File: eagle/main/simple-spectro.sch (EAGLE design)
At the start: 50 parts, among them IC1 MCP1703-33, Q1 DMP1045U, U1 MCP73831T, X2 8MHz, X4 MINI-USB

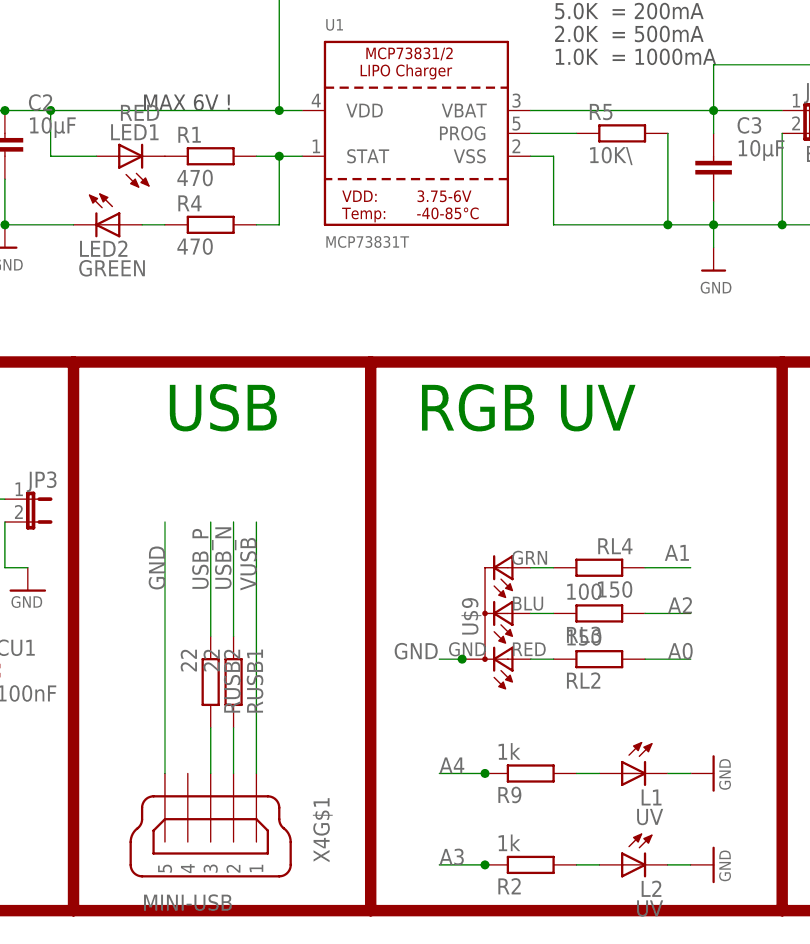
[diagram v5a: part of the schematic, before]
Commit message: update pcb values
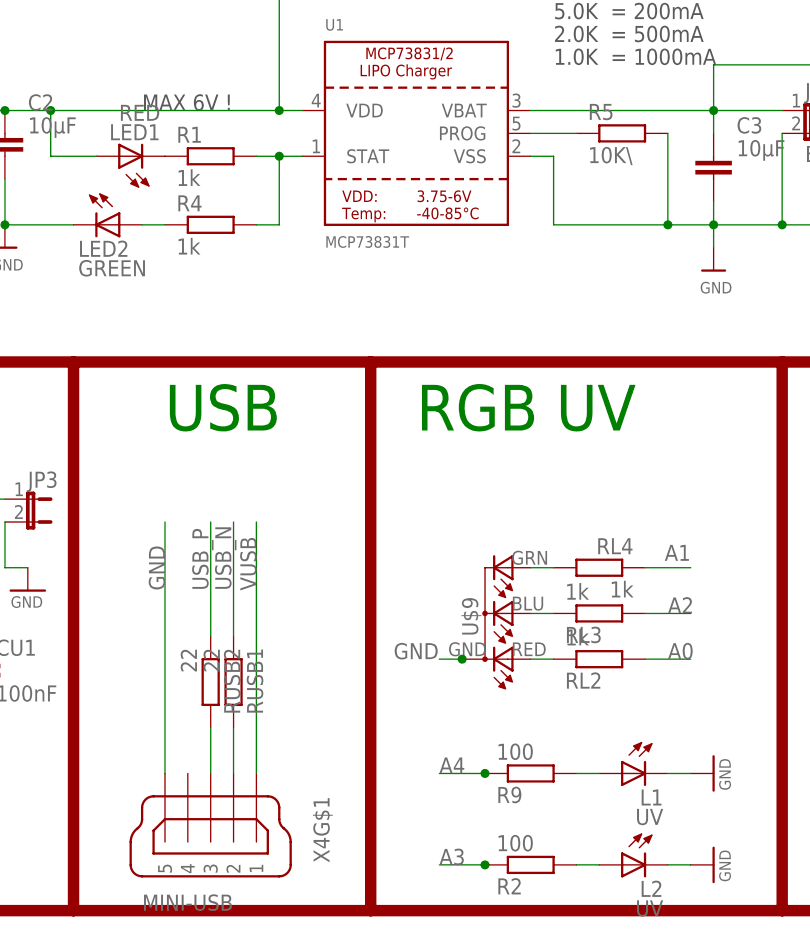
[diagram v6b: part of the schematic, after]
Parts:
- R1, R4: value 470 -> 1k
- R2, R9: value 1k -> 100
- RL2, RL4: value 150 -> 1k
- RL3: value 100 -> 1k
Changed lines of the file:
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@@
 <part name="LED1" library="SparkFun" deviceset="LED" device="1206" value="RED"/>
 <part name="LED2" library="SparkFun" deviceset="LED" device="1206" value="GREEN"/>
-<part name="R1" library="rcl" deviceset="R-EU_" device="M1206" package3d_urn="urn:adsk.eagle:package:23566/1" value="470"/>
-<part name="R4" library="rcl" deviceset="R-EU_" device="M1206" package3d_urn="urn:adsk.eagle:package:23566/1" value="470"/>
+<part name="R1" library="rcl" deviceset="R-EU_" device="M1206" package3d_urn="urn:adsk.eagle:package:23566/1" value="1k"/>
+<part name="R4" library="rcl" deviceset="R-EU_" device="M1206" package3d_urn="urn:adsk.eagle:package:23566/1" value="1k"/>
 <part name="C2" library="dp_devices" deviceset="CAPACITOR_NPOL" device="-1206" value="10µF"/>
 <part name="U$3" library="microbuilder" deviceset="GND" device=""/>
@@
 <part name="U$5" library="microbuilder" deviceset="GND" device=""/>
 <part name="R5" library="rcl" deviceset="R-EU_" device="M1206" package3d_urn="urn:adsk.eagle:package:23566/1" value="10K\"/>
-<part name="RL2" library="rcl" deviceset="R-EU_" device="M1206" value="150"/>
-<part name="RL3" library="rcl" deviceset="R-EU_" device="M1206" value="100"/>
-<part name="RL4" library="rcl" deviceset="R-EU_" device="M1206" value="150"/>
+<part name="RL2" library="rcl" deviceset="R-EU_" device="M1206" value="1k"/>
+<part name="RL3" library="rcl" deviceset="R-EU_" device="M1206" value="1k"/>
+<part name="RL4" library="rcl" deviceset="R-EU_" device="M1206" value="1k"/>
 <part name="U$9" library="lpatiny" deviceset="RGB-COMMON-CATHODE" device=""/>
 <part name="U$11" library="HD44780LCD" deviceset="LCD-HD44780" device="16X2-4-HOLES" technology="4-HOLES"/>
@@
 <part name="U$2" library="MyPOW" deviceset="VUSB" device=""/>
 <part name="D4" library="lpatiny" deviceset="1N581*" device="D1206" value="1N581D1206"/>
-<part name="R9" library="rcl" deviceset="R-EU_" device="M1206" value="1k"/>
+<part name="R9" library="rcl" deviceset="R-EU_" device="M1206" value="100"/>
 <part name="GND9" library="supply1" deviceset="GND" device=""/>
 <part name="L1" library="SparkFun" deviceset="LED" device="5MM" value="UV"/>
@@
 <part name="CU1" library="resistor" library_urn="urn:adsk.eagle:library:348" deviceset="C-EU" device="C1206" package3d_urn="urn:adsk.eagle:package:26140/1" value="100nF"/>
 <part name="RK3" library="rcl" library_urn="urn:adsk.eagle:library:334" deviceset="R-EU_" device="M1206" package3d_urn="urn:adsk.eagle:package:23566/1" value="100k"/>
-<part name="R2" library="rcl" deviceset="R-EU_" device="M1206" value="1k"/>
+<part name="R2" library="rcl" deviceset="R-EU_" device="M1206" value="100"/>
 <part name="GND10" library="supply1" deviceset="GND" device=""/>
 <part name="L2" library="led" deviceset="LED" device="3MM" value="UV"/>

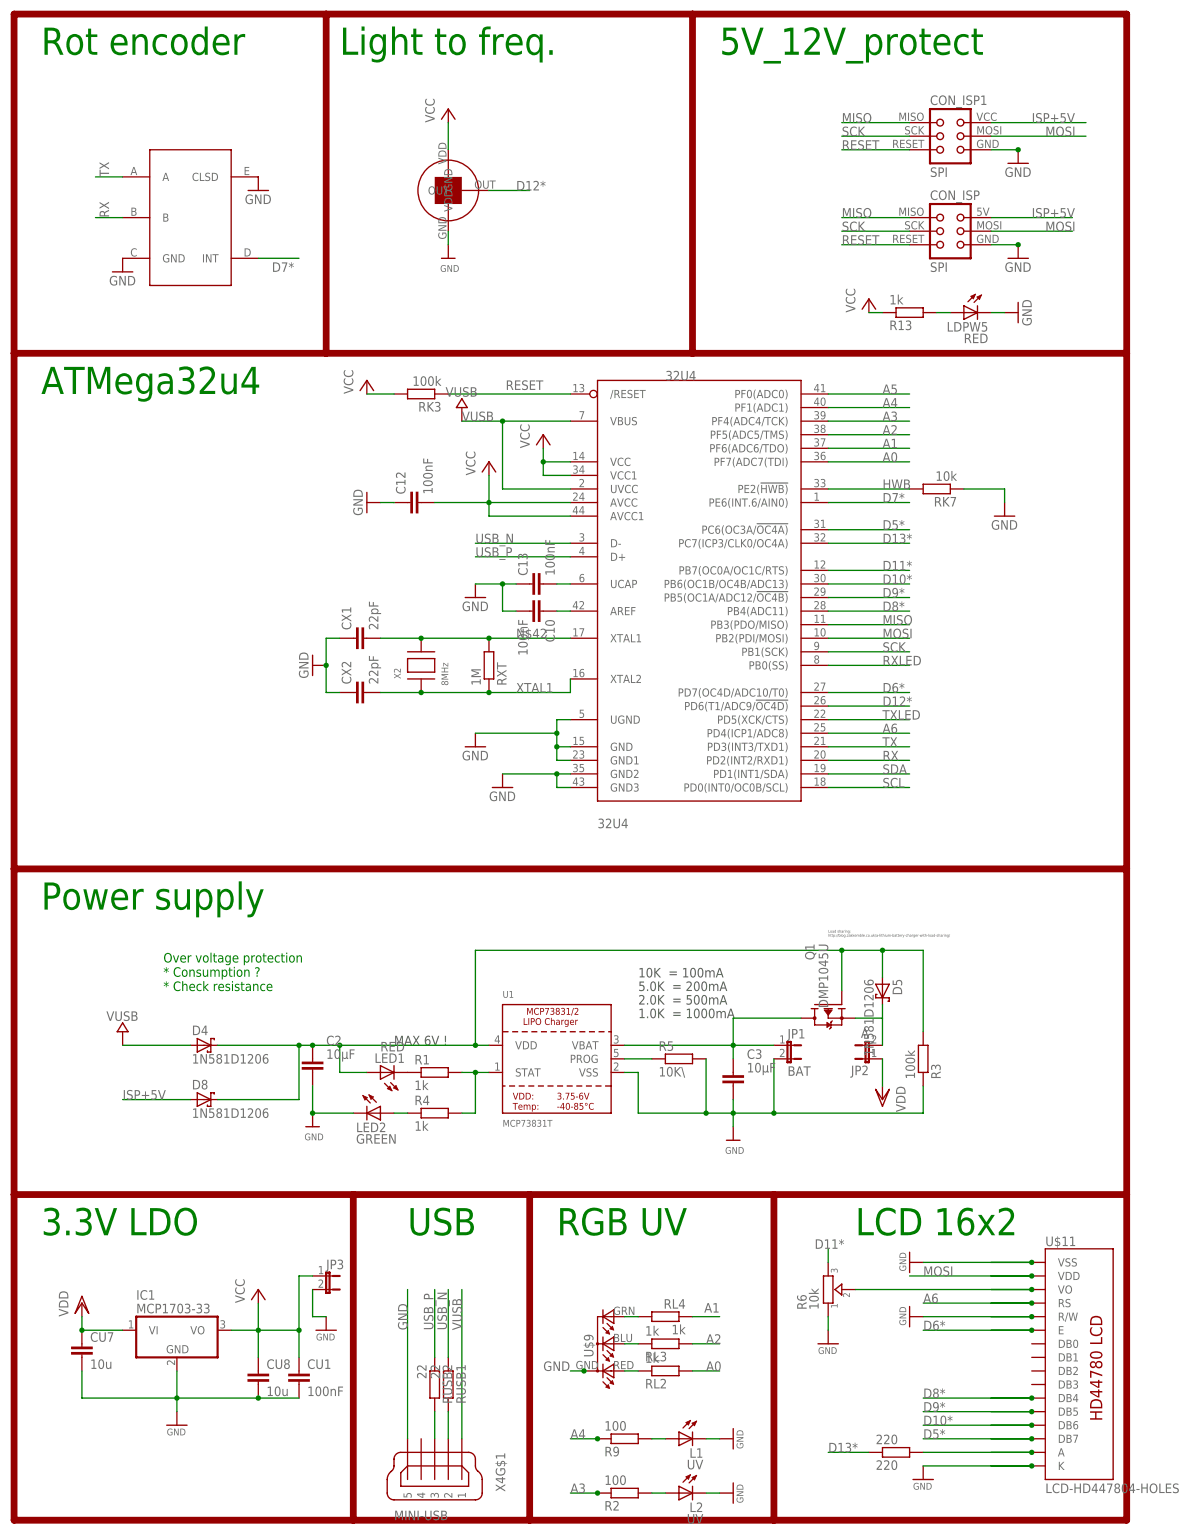
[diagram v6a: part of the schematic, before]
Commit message: add manufacturer references for BOM
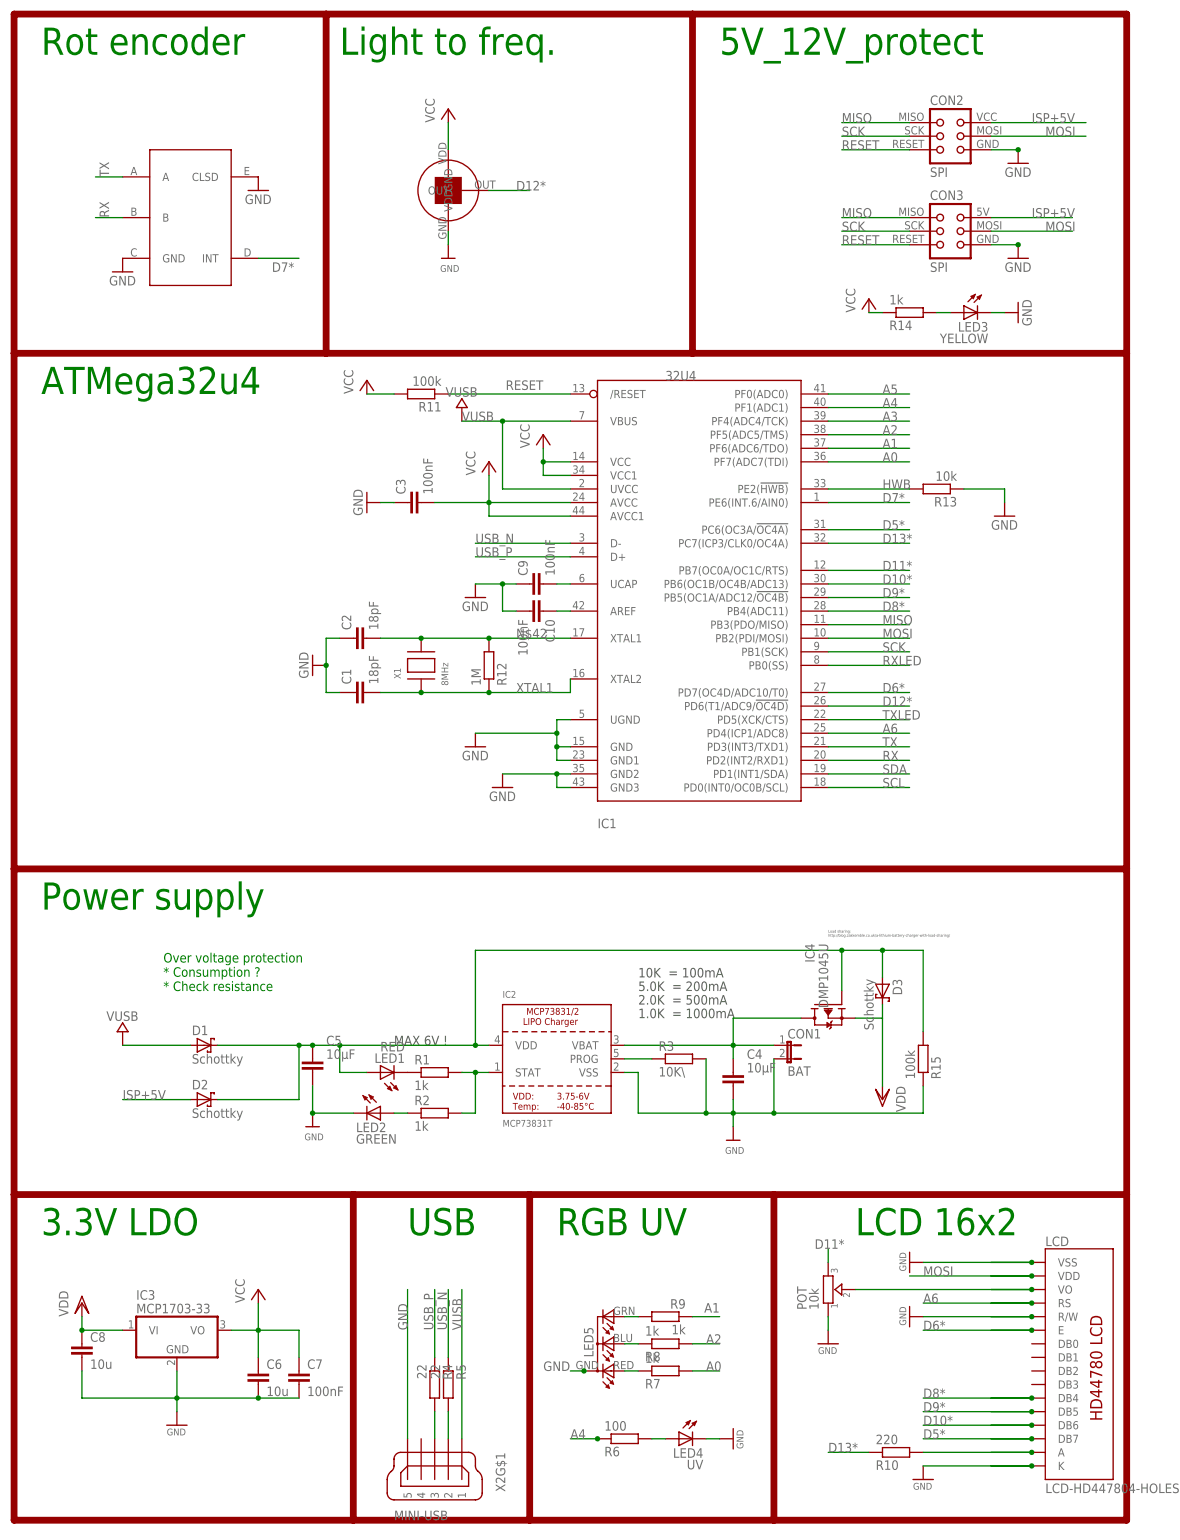
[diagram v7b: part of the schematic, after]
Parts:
- removed 32U4: 32U4, adafruit:ATMEGA32U4-AU
- removed C12: 100nF, resistor:C-EUC1206
- removed CX1: 22pF, resistor:C-EUC1206
- removed JP2: A, jumper:JP1E
- removed JP3: (no value), jumper:JP1E
- removed L2: UV, led:LED3MM
- removed RK7: 10k, rcl:R-EU_M1206
- removed RL4: 1k, rcl:R-EU_M1206
- removed RUSB1, RUSB2: 22, rcl:R-EU_M1206
- removed X4: MINI-USB, con-cypressindustries:MINI-USB-SCHIELD-32005-201
- added C4, C5: 10µF, dp_devices:CAPACITOR_NPOL-1206
- added IC3: MCP1703-33, linear:MCP1703DB
- added POT: 10k, dp_devices:TRIMMER-3362P
- added R14: 1k, rcl:R-EU_M1206
- added R15: 100k, rcl:R-EU_M1206
- added X1: 8MHz, lpatiny:XTALNX6035
- C1: value 22pF -> 18pF; MPN (none) -> 77-VJ1206A180JXXPBC
- C10, C7, C9: MPN (none) -> 80-C1206C104K5R
- C2: value 10µF -> 18pF; device dp_devices:CAPACITOR_NPOL-1206 -> resistor:C-EUC1206; MPN (none) -> 77-VJ1206A180JXXPBC
- C3: value 10µF -> 100nF; device dp_devices:CAPACITOR_NPOL-1206 -> resistor:C-EUC1206; MPN (none) -> 80-C1206C104K5R
- C6, C8: MPN (none) -> 77-VJ1206V106MXQTBC
- D1, D2, D3: value 1N581D1206 -> Schottky; MPN (none) -> 579-MCP1703-3302E/DB
- IC1: value MCP1703-33 -> 32U4; device linear:MCP1703DB -> adafruit:ATMEGA32U4-AU; MPN (none) -> 556-ATMEGA32U4RC-AU
- IC2: MPN (none) -> 579-MCP73831T-3ACIOT
- IC4: MPN (none) -> 621-DMP1045U-7
- LED1: MPN (none) -> 604-APT3216EC
- LED2: MPN (none) -> 604-APTR3216SGC
- LED3: value RED -> YELLOW; MPN (none) -> 604-APTR3216YC
- R1, R7, R8: MPN (none) -> 667-ERJ-8GEYJ101V
- R10: MPN (none) -> 667-ERJ-U08J221V
- R11: MPN (none) -> RC1206FR-07100KL
- R12: MPN (none) -> ERJ-8GEYJ105V
- R13: value 1k -> 10k; MPN (none) -> 603-RC1206FR-0710KL
- R2, R9: value 100 -> 1k; MPN (none) -> 667-ERJ-8GEYJ101V
- R3: value 100k -> 10K\; MPN (none) -> 603-RC1206FR-0710KL
- R4: value 1k -> 22; MPN (none) -> 603-RC1206FR-0722RL
- R5: value 10K\ -> 22; MPN (none) -> 603-RC1206FR-0722RL
- R6: value 10k -> 100; device dp_devices:TRIMMER-3362P -> rcl:R-EU_M1206; MPN (none) -> 667-ERJ-8GEYJ101V
- X2: value 8MHz -> MINI-USB; device lpatiny:XTALNX6035 -> con-cypressindustries:MINI-USB-SCHIELD-32005-201; MPN (none) -> 649-10033526-N3212LF
- renumbered 220 to R10, C13 to C9, CON_ISP to CON3, CON_ISP1 to CON2, CU1 to C7, CU7 to C8, CU8 to C6, CX2 to C1, D4 to D1, D5 to D3, D8 to D2, JP1 to CON1, L1 to LED4, LDPW5 to LED3, Q1 to IC4, RK3 to R11, RL2 to R7, RL3 to R8, RXT to R12, U$11 to LCD, U$9 to LED5, U1 to IC2
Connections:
- removed net N$17: D3.C, IC4.S, JP2.2
- removed net N$8: L2.A, R2.2
- net A0: now also IC1.PF7(ADC7(TDI); no longer 32U4.PF7(ADC7(TDI)
- net A1: now also IC1.PF6(ADC6/TDO), R9.1; no longer 32U4.PF6(ADC6/TDO), RL4.1
- net A2: now also IC1.PF5(ADC5/TMS); no longer 32U4.PF5(ADC5/TMS)
- net A3: now also IC1.PF4(ADC4/TCK); no longer 32U4.PF4(ADC4/TCK), R2.1
- net A4: now also IC1.PF1(ADC1), R6.1; no longer 32U4.PF1(ADC1), R9.1
- net A5: now also IC1.PF0(ADC0); no longer 32U4.PF0(ADC0)
- net A6: now also IC1.PD4(ICP1/ADC8); no longer 32U4.PD4(ICP1/ADC8)
- net AREF: now also IC1.AREF; no longer 32U4.AREF
- net D10*: now also IC1.PB6(OC1B/OC4B/ADC13); no longer 32U4.PB6(OC1B/OC4B/ADC13)
- net D11*: now also IC1.PB7(OC0A/OC1C/RTS), POT.3; no longer 32U4.PB7(OC0A/OC1C/RTS), R6.3
- net D12*: now also IC1.PD6(T1/ADC9/!OC4D); no longer 32U4.PD6(T1/ADC9/!OC4D)
- net D13*: now also IC1.PC7(ICP3/CLK0/OC4A); no longer 32U4.PC7(ICP3/CLK0/OC4A)
- net D5*: now also IC1.PC6(OC3A/!OC4A); no longer 32U4.PC6(OC3A/!OC4A)
- net D6*: now also IC1.PD7(OC4D/ADC10/T0); no longer 32U4.PD7(OC4D/ADC10/T0)
- net D7*: now also IC1.PE6(INT.6/AIN0); no longer 32U4.PE6(INT.6/AIN0)
- net D8*: now also IC1.PB4(ADC11); no longer 32U4.PB4(ADC11)
- net D9*: now also IC1.PB5(OC1A/ADC12/!OC4B); no longer 32U4.PB5(OC1A/ADC12/!OC4B)
- net GND: now also C2.1, C3.1, C4.2, C5.2, IC1.GND1, IC1.GND2, IC1.GND3, IC1.UGND, IC3.GND, POT.1, R13.1, R15.1, R3.2, X2G$1.5; no longer 32U4.GND, 32U4.GND1, 32U4.GND2, 32U4.GND3, 32U4.UGND, C12.1, C2.2, C3.2, CX1.1, JP3.2, L2.C, R3.1, R5.2, R6.1, RK7.1, X4G$1.5
- net HWB: now also IC1.PE2(!HWB), R13.2; no longer 32U4.PE2(!HWB), RK7.2
- net MISO: now also IC1.PB3(PDO/MISO); no longer 32U4.PB3(PDO/MISO)
- net MOSI: now also IC1.PB2(PDI/MOSI); no longer 32U4.PB2(PDI/MOSI)
- net N$1: now also IC1.UCAP; no longer 32U4.UCAP
- net N$12: now also R14.2; no longer R13.2
- net N$15: now also C5.1, R15.2; no longer C2.1, R3.2
- net N$2: now also POT.2; no longer R6.2
- net N$3: now also R6.2; no longer R9.2
- net N$42: now also C2.2, IC1.XTAL1, X1.P$2; no longer 32U4.XTAL1, CX1.2, X2.P$2
- net N$5: now also R2.2; no longer R4.2
- net N$6: now also R3.1; no longer R5.1
- net N$7: now also R2.1; no longer R4.1
- net N$9: now also R9.2; no longer RL4.2
- net RESET: now also IC1./RESET; no longer 32U4./RESET
- net RX: now also IC1.PD2(INT2/RXD1); no longer 32U4.PD2(INT2/RXD1)
- net RXLED: now also IC1.PB0(SS); no longer 32U4.PB0(SS)
- net SCK: now also IC1.PB1(SCK); no longer 32U4.PB1(SCK)
- net SCL: now also IC1.PD0(INT0/OC0B/SCL); no longer 32U4.PD0(INT0/OC0B/SCL)
- net SDA: now also IC1.PD1(INT1/SDA); no longer 32U4.PD1(INT1/SDA)
- net TX: now also IC1.PD3(INT3/TXD1); no longer 32U4.PD3(INT3/TXD1)
- net TXLED: now also IC1.PD5(XCK/CTS); no longer 32U4.PD5(XCK/CTS)
- net USBC_N: now also R5.2, X2G$1.2; no longer RUSB1.2, X4G$1.2
- net USBC_P: now also R4.2, X2G$1.3; no longer RUSB2.2, X4G$1.3
- net USB_N: now also IC1.D-, R5.1; no longer 32U4.D-, RUSB1.1
- net USB_P: now also IC1.D+, R4.1; no longer 32U4.D+, RUSB2.1
- net VBAT1: now also C4.1; no longer C3.1
- net VCC: now also C3.2, IC1.AVCC, IC1.AVCC1, IC1.VCC, IC1.VCC1, IC3.VO, R14.1; no longer 32U4.AVCC, 32U4.AVCC1, 32U4.VCC, 32U4.VCC1, C12.2, IC1.VO, JP3.1, R13.1
- net VDD: now also D3.C, IC3.VI, IC4.S; no longer IC1.VI, JP2.1
- net VUSB: now also IC1.UVCC, IC1.VBUS, X2G$1.1; no longer 32U4.UVCC, 32U4.VBUS, X4G$1.1
- net XTAL1: now also IC1.XTAL2, X1.P$1; no longer 32U4.XTAL2, X2.P$1
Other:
- moved on the sheet: R13, R2, R3, R4, R5, R9

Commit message: add files for new price offer with assembly
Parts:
- C4, C5: value 10µF -> 10u
- R3: value 10K\ -> 10K
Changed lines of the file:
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@@
 <attribute name="MPN" value="667-ERJ-8GEYJ101V"/>
 </part>
-<part name="C5" library="dp_devices" deviceset="CAPACITOR_NPOL" device="-1206" value="10µF">
+<part name="C5" library="dp_devices" deviceset="CAPACITOR_NPOL" device="-1206" value="10u">
 <attribute name="MPN" value="77-VJ1206V106MXQTBC"/>
 </part>
 <part name="U$3" library="microbuilder" deviceset="GND" device=""/>
-<part name="C4" library="dp_devices" deviceset="CAPACITOR_NPOL" device="-1206" value="10µF">
+<part name="C4" library="dp_devices" deviceset="CAPACITOR_NPOL" device="-1206" value="10u">
 <attribute name="MPN" value="77-VJ1206V106MXQTBC"/>
 </part>
 <part name="U$5" library="microbuilder" deviceset="GND" device=""/>
-<part name="R3" library="rcl" deviceset="R-EU_" device="M1206" value="10K\">
+<part name="R3" library="rcl" deviceset="R-EU_" device="M1206" value="10K">
 <attribute name="MPN" value="603-RC1206FR-0710KL"/>
 </part>
